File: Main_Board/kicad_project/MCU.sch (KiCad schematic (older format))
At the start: 3 parts

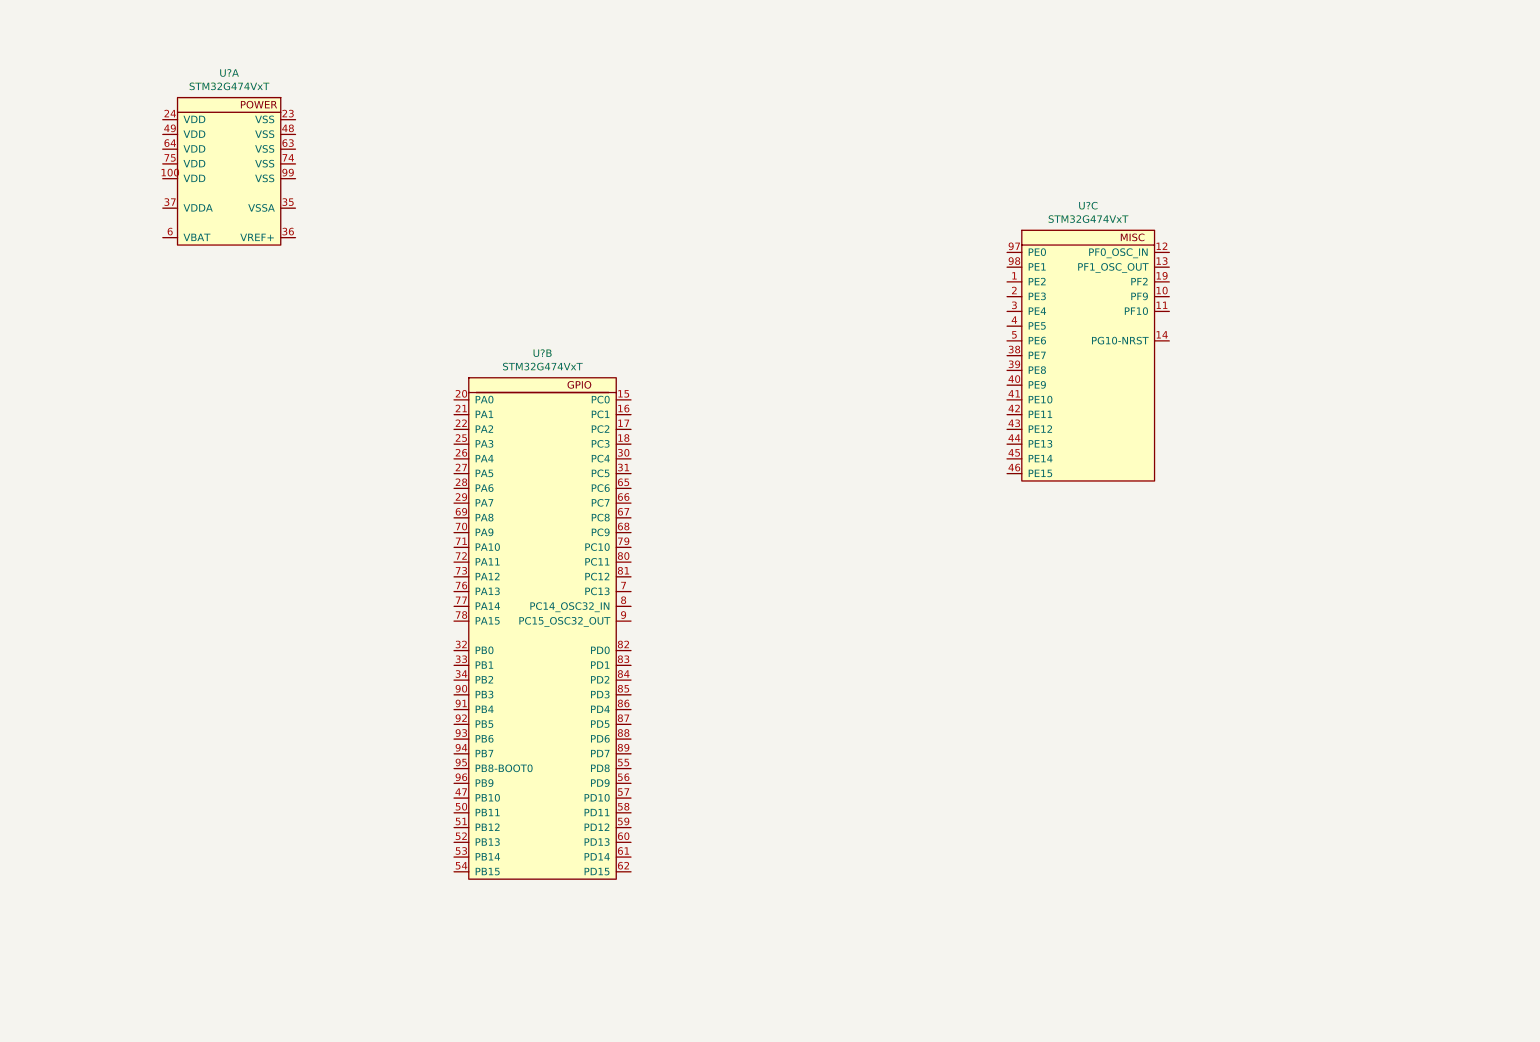
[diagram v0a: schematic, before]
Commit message: add input/output schematic, add documentation
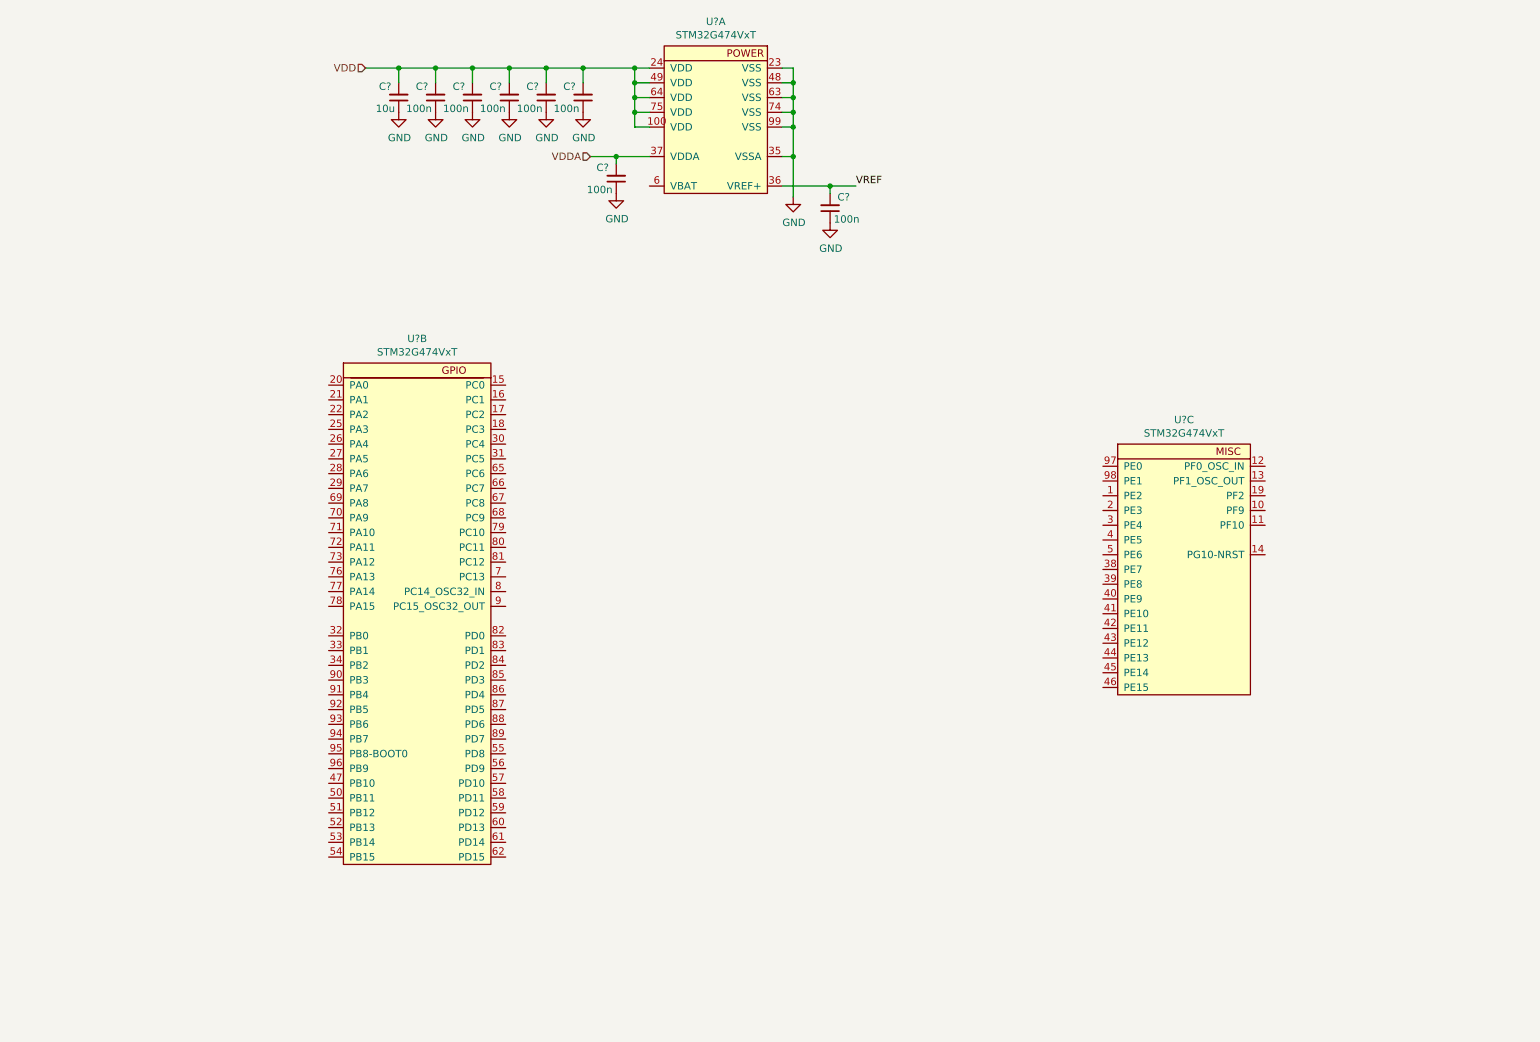
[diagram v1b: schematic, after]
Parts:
- added C? (x7): 100n, Capacitor_SMD:C_0603_1608Metric, symbol Device:C_Small
- added C?: 10u, Capacitor_SMD:C_1210_3225Metri, symbol Device:C_Small
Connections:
- net VDD: now reaches U?.100 (VDD)
- net VDD: now also U?.24 (VDD), U?.49 (VDD), U?.64 (VDD), U?.75 (VDD), C?.2, C?.2, C?.2, C?.2, C?.2, C?.2
- net GND: now reaches U?.23 (VSS)
- net GND: now also U?.35 (VSSA), U?.48 (VSS), U?.63 (VSS), U?.74 (VSS), U?.99 (VSS), C?.1, C?.1, C?.1, C?.1, C?.1, C?.1, C?.1, C?.1
- net VREF: now reaches U?.36 (VREF+)
- net VREF: now also C?.2
- net VDDA: now reaches U?.37 (VDDA)
- net VDDA: now also C?.2
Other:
- moved on the sheet: U?A, U?B, U?C

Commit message: add external IO
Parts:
- C?: footprint Capacitor_SMD:C_1210_3225Metri -> Capacitor_SMD:C_1210_3225Metric
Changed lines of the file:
@@
 $Descr A4 11693 8268
 encoding utf-8
-Sheet 7 8
+Sheet 7 9
 Title ""
 Date ""
@@
 F 0 "C?" H 3275 975 50  0000 R CNN
 F 1 "10u" H 3300 1125 50  0000 R CNN
-F 2 "Capacitor_SMD:C_1210_3225Metri" H 3325 1050 50  0001 C CNN
+F 2 "Capacitor_SMD:C_1210_3225Metric" H 3325 1050 50  0001 C CNN
 F 3 "~" H 3325 1050 50  0001 C CNN
 	1    3325 1050

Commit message: progress?
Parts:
- gave numbers to parts that had none: 9
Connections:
- net USB_DM: now reaches U7.72 (PA11)
- net USB_DP: now reaches U7.73 (PA12)
- net SWDIO_JTMS: now reaches U7.76 (PA13)
- net SWCLK_JTCK: now reaches U7.77 (PA14)
- net JDI: now reaches U7.78 (PA15)
- net JTDO_TRACESWO: now reaches U7.90 (PB3)
- net JTRST: now reaches U7.91 (PB4)
- net NRST: now reaches U7.14 (PG10-NRST)
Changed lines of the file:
@@
 $EndDescr
 $Comp
-L LoaDy:STM32G474VxT U?
+L LoaDy:STM32G474VxT U7
 U 1 1 5F5465C4
 P 5475 1250
-F 0 "U?" H 5475 1965 50  0000 C CNN
+F 0 "U7" H 5475 1965 50  0000 C CNN
 F 1 "STM32G474VxT" H 5475 1874 50  0000 C CNN
 F 2 "Package_QFP:LQFP-100_14x14mm_P0.5mm" H 5475 1950 50  0001 C CNN
@@
 $EndComp
 $Comp
-L LoaDy:STM32G474VxT U?
+L LoaDy:STM32G474VxT U7
 U 2 1 5F547F4E
 P 3450 3400
-F 0 "U?" H 3450 4115 50  0000 C CNN
+F 0 "U7" H 3450 4115 50  0000 C CNN
 F 1 "STM32G474VxT" H 3450 4024 50  0000 C CNN
 F 2 "Package_QFP:LQFP-100_14x14mm_P0.5mm" H 3450 4100 50  0001 C CNN
@@
 $EndComp
 $Comp
-L LoaDy:STM32G474VxT U?
+L LoaDy:STM32G474VxT U7
 U 3 1 5F54AE3E
 P 8650 3950
-F 0 "U?" H 8650 4665 50  0000 C CNN
+F 0 "U7" H 8650 4665 50  0000 C CNN
 F 1 "STM32G474VxT" H 8650 4574 50  0000 C CNN
 F 2 "Package_QFP:LQFP-100_14x14mm_P0.5mm" H 8650 4650 50  0001 C CNN
@@
 $EndComp
 $Comp
-L Device:C_Small C?
+L Device:C_Small C60
 U 1 1 5F50168E
 P 4575 1050
-F 0 "C?" H 4525 975 50  0000 R CNN
+F 0 "C60" H 4525 975 50  0000 R CNN
 F 1 "100n" H 4550 1125 50  0000 R CNN
 F 2 "Capacitor_SMD:C_0603_1608Metric" H 4575 1050 50  0001 C CNN
@@
 $EndComp
 $Comp
-L Device:C_Small C?
+L Device:C_Small C59
 U 1 1 5F503E90
 P 4325 1050
-F 0 "C?" H 4275 975 50  0000 R CNN
+F 0 "C59" H 4275 975 50  0000 R CNN
 F 1 "100n" H 4300 1125 50  0000 R CNN
 F 2 "Capacitor_SMD:C_0603_1608Metric" H 4325 1050 50  0001 C CNN
@@
 $EndComp
 $Comp
-L Device:C_Small C?
+L Device:C_Small C58
 U 1 1 5F504272
 P 4075 1050
-F 0 "C?" H 4025 975 50  0000 R CNN
+F 0 "C58" H 4025 975 50  0000 R CNN
 F 1 "100n" H 4050 1125 50  0000 R CNN
 F 2 "Capacitor_SMD:C_0603_1608Metric" H 4075 1050 50  0001 C CNN
@@
 $EndComp
 $Comp
-L Device:C_Small C?
+L Device:C_Small C57
 U 1 1 5F50454D
 P 3825 1050
-F 0 "C?" H 3775 975 50  0000 R CNN
+F 0 "C57" H 3775 975 50  0000 R CNN
 F 1 "100n" H 3800 1125 50  0000 R CNN
 F 2 "Capacitor_SMD:C_0603_1608Metric" H 3825 1050 50  0001 C CNN
@@
 $EndComp
 $Comp
-L Device:C_Small C?
+L Device:C_Small C56
 U 1 1 5F504BCE
 P 3575 1050
-F 0 "C?" H 3525 975 50  0000 R CNN
+F 0 "C56" H 3525 975 50  0000 R CNN
 F 1 "100n" H 3550 1125 50  0000 R CNN
 F 2 "Capacitor_SMD:C_0603_1608Metric" H 3575 1050 50  0001 C CNN
@@
 $EndComp
 $Comp
-L Device:C_Small C?
+L Device:C_Small C55
 U 1 1 5F505049
 P 3325 1050
-F 0 "C?" H 3275 975 50  0000 R CNN
+F 0 "C55" H 3275 975 50  0000 R CNN
 F 1 "10u" H 3300 1125 50  0000 R CNN
 F 2 "Capacitor_SMD:C_1210_3225Metric" H 3325 1050 50  0001 C CNN
@@
 	4925 1150 4925 1050
 $Comp
-L power:GND #PWR?
+L power:GND #PWR050
 U 1 1 5F508D68
 P 4575 1150
-F 0 "#PWR?" H 4575 900 50  0001 C CNN
+F 0 "#PWR050" H 4575 900 50  0001 C CNN
 F 1 "GND" H 4580 977 50  0000 C CNN
 F 2 "" H 4575 1150 50  0001 C CNN
@@
 $EndComp
 $Comp
-L power:GND #PWR?
+L power:GND #PWR049
 U 1 1 5F5090A8
 P 4325 1150
-F 0 "#PWR?" H 4325 900 50  0001 C CNN
+F 0 "#PWR049" H 4325 900 50  0001 C CNN
 F 1 "GND" H 4330 977 50  0000 C CNN
 F 2 "" H 4325 1150 50  0001 C CNN
@@
 $EndComp
 $Comp
-L power:GND #PWR?
+L power:GND #PWR048
 U 1 1 5F5092B8
 P 4075 1150
-F 0 "#PWR?" H 4075 900 50  0001 C CNN
+F 0 "#PWR048" H 4075 900 50  0001 C CNN
 F 1 "GND" H 4080 977 50  0000 C CNN
 F 2 "" H 4075 1150 50  0001 C CNN
@@
 $EndComp
 $Comp
-L power:GND #PWR?
+L power:GND #PWR047
 U 1 1 5F509567
 P 3825 1150
-F 0 "#PWR?" H 3825 900 50  0001 C CNN
+F 0 "#PWR047" H 3825 900 50  0001 C CNN
 F 1 "GND" H 3830 977 50  0000 C CNN
 F 2 "" H 3825 1150 50  0001 C CNN
@@
 $EndComp
 $Comp
-L power:GND #PWR?
+L power:GND #PWR046
 U 1 1 5F5097C9
 P 3575 1150
-F 0 "#PWR?" H 3575 900 50  0001 C CNN
+F 0 "#PWR046" H 3575 900 50  0001 C CNN
 F 1 "GND" H 3580 977 50  0000 C CNN
 F 2 "" H 3575 1150 50  0001 C CNN
@@
 $EndComp
 $Comp
-L power:GND #PWR?
+L power:GND #PWR045
 U 1 1 5F50999B
 P 3325 1150
-F 0 "#PWR?" H 3325 900 50  0001 C CNN
+F 0 "#PWR045" H 3325 900 50  0001 C CNN
 F 1 "GND" H 3330 977 50  0000 C CNN
 F 2 "" H 3325 1150 50  0001 C CNN
@@
 VDD
 $Comp
-L Device:C_Small C?
+L Device:C_Small C61
 U 1 1 5F509E58
 P 4800 1600
-F 0 "C?" H 4750 1525 50  0000 R CNN
+F 0 "C61" H 4750 1525 50  0000 R CNN
 F 1 "100n" H 4775 1675 50  0000 R CNN
 F 2 "Capacitor_SMD:C_0603_1608Metric" H 4800 1600 50  0001 C CNN
@@
 $EndComp
 $Comp
-L power:GND #PWR?
+L power:GND #PWR051
 U 1 1 5F50A4F3
 P 4800 1700
-F 0 "#PWR?" H 4800 1450 50  0001 C CNN
+F 0 "#PWR051" H 4800 1450 50  0001 C CNN
 F 1 "GND" H 4805 1527 50  0000 C CNN
 F 2 "" H 4800 1700 50  0001 C CNN
@@
 VDDA
 $Comp
-L power:GND #PWR?
+L power:GND #PWR052
 U 1 1 5F513C8D
 P 6000 1725
-F 0 "#PWR?" H 6000 1475 50  0001 C CNN
+F 0 "#PWR052" H 6000 1475 50  0001 C CNN
 F 1 "GND" H 6005 1552 50  0000 C CNN
 F 2 "" H 6000 1725 50  0001 C CNN
@@
 	6000 1450 6000 1250
 $Comp
-L Device:C_Small C?
+L Device:C_Small C62
 U 1 1 5F517AF6
 P 6250 1800
-F 0 "C?" H 6200 1725 50  0000 R CNN
+F 0 "C62" H 6200 1725 50  0000 R CNN
 F 1 "100n" H 6225 1875 50  0000 R CNN
 F 2 "Capacitor_SMD:C_0603_1608Metric" H 6250 1800 50  0001 C CNN
@@
 	5925 1650 6250 1650
 $Comp
-L power:GND #PWR?
+L power:GND #PWR053
 U 1 1 5F51901D
 P 6250 1900
-F 0 "#PWR?" H 6250 1650 50  0001 C CNN
+F 0 "#PWR053" H 6250 1650 50  0001 C CNN
 F 1 "GND" H 6255 1727 50  0000 C CNN
 F 2 "" H 6250 1900 50  0001 C CNN
@@
 Text Label 6425 1650 0    50   ~ 0
 VREF
+Wire Wire Line
+	2850 4100 2500 4100
+Wire Wire Line
+	2850 4200 2500 4200
+Text Label 2725 4100 2    50   ~ 0
+USB_DM
+Text Label 2700 4200 2    50   ~ 0
+USB_DP
+Wire Wire Line
+	2850 4300 2500 4300
+Wire Wire Line
+	2850 4400 2500 4400
+Text Label 2500 4300 2    50   ~ 0
+SWDIO_JTMS
+Text Label 2500 4400 2    50   ~ 0
+SWCLK_JTCK
+Wire Wire Line
+	2500 4500 2850 4500
+Text Label 2500 4500 2    50   ~ 0
+JDI
+Wire Wire Line
+	2850 5000 2500 5000
+Text Label 2500 5000 2    50   ~ 0
+JTDO_TRACESWO
+Wire Wire Line
+	2850 5100 2500 5100
+Text Label 2500 5100 2    50   ~ 0
+JTRST
+Wire Wire Line
+	9200 4150 9450 4150
+Text Label 9450 4150 0    50   ~ 0
+NRST
+Entry Wire Line
+	2500 4100 2400 4000
+Entry Wire Line
+	2500 4200 2400 4100
+Wire Bus Line
+	2400 3875 2300 3875
+Wire Bus Line
+	2400 3875 2400 4100
+Text HLabel 2300 3875 0    50   BiDi ~ 10
+USB
 $EndSCHEMATC

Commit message: progress on MCU pinout
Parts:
- renumbered C60 to C?, C59 to C?, C58 to C?, C57 to C?, C56 to C?, C55 to C?, C61 to C?, C62 to C?, U7 to U?
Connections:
- net MCO: now reaches U?.69 (PA8)
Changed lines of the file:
@@
 $EndDescr
 $Comp
-L LoaDy:STM32G474VxT U7
+L LoaDy:STM32G474VxT U?
 U 1 1 5F5465C4
 P 5475 1250
-F 0 "U7" H 5475 1965 50  0000 C CNN
+F 0 "U?" H 5475 1965 50  0000 C CNN
 F 1 "STM32G474VxT" H 5475 1874 50  0000 C CNN
 F 2 "Package_QFP:LQFP-100_14x14mm_P0.5mm" H 5475 1950 50  0001 C CNN
@@
 $EndComp
 $Comp
-L LoaDy:STM32G474VxT U7
+L LoaDy:STM32G474VxT U?
 U 2 1 5F547F4E
 P 3450 3400
-F 0 "U7" H 3450 4115 50  0000 C CNN
+F 0 "U?" H 3450 4115 50  0000 C CNN
 F 1 "STM32G474VxT" H 3450 4024 50  0000 C CNN
 F 2 "Package_QFP:LQFP-100_14x14mm_P0.5mm" H 3450 4100 50  0001 C CNN
@@
 $EndComp
 $Comp
-L LoaDy:STM32G474VxT U7
+L LoaDy:STM32G474VxT U?
 U 3 1 5F54AE3E
 P 8650 3950
-F 0 "U7" H 8650 4665 50  0000 C CNN
+F 0 "U?" H 8650 4665 50  0000 C CNN
 F 1 "STM32G474VxT" H 8650 4574 50  0000 C CNN
 F 2 "Package_QFP:LQFP-100_14x14mm_P0.5mm" H 8650 4650 50  0001 C CNN
@@
 $EndComp
 $Comp
-L Device:C_Small C60
+L Device:C_Small C?
 U 1 1 5F50168E
 P 4575 1050
-F 0 "C60" H 4525 975 50  0000 R CNN
+F 0 "C?" H 4525 975 50  0000 R CNN
 F 1 "100n" H 4550 1125 50  0000 R CNN
 F 2 "Capacitor_SMD:C_0603_1608Metric" H 4575 1050 50  0001 C CNN
@@
 $EndComp
 $Comp
-L Device:C_Small C59
+L Device:C_Small C?
 U 1 1 5F503E90
 P 4325 1050
-F 0 "C59" H 4275 975 50  0000 R CNN
+F 0 "C?" H 4275 975 50  0000 R CNN
 F 1 "100n" H 4300 1125 50  0000 R CNN
 F 2 "Capacitor_SMD:C_0603_1608Metric" H 4325 1050 50  0001 C CNN
@@
 $EndComp
 $Comp
-L Device:C_Small C58
+L Device:C_Small C?
 U 1 1 5F504272
 P 4075 1050
-F 0 "C58" H 4025 975 50  0000 R CNN
+F 0 "C?" H 4025 975 50  0000 R CNN
 F 1 "100n" H 4050 1125 50  0000 R CNN
 F 2 "Capacitor_SMD:C_0603_1608Metric" H 4075 1050 50  0001 C CNN
@@
 $EndComp
 $Comp
-L Device:C_Small C57
+L Device:C_Small C?
 U 1 1 5F50454D
 P 3825 1050
-F 0 "C57" H 3775 975 50  0000 R CNN
+F 0 "C?" H 3775 975 50  0000 R CNN
 F 1 "100n" H 3800 1125 50  0000 R CNN
 F 2 "Capacitor_SMD:C_0603_1608Metric" H 3825 1050 50  0001 C CNN
@@
 $EndComp
 $Comp
-L Device:C_Small C56
+L Device:C_Small C?
 U 1 1 5F504BCE
 P 3575 1050
-F 0 "C56" H 3525 975 50  0000 R CNN
+F 0 "C?" H 3525 975 50  0000 R CNN
 F 1 "100n" H 3550 1125 50  0000 R CNN
 F 2 "Capacitor_SMD:C_0603_1608Metric" H 3575 1050 50  0001 C CNN
@@
 $EndComp
 $Comp
-L Device:C_Small C55
+L Device:C_Small C?
 U 1 1 5F505049
 P 3325 1050
-F 0 "C55" H 3275 975 50  0000 R CNN
+F 0 "C?" H 3275 975 50  0000 R CNN
 F 1 "10u" H 3300 1125 50  0000 R CNN
 F 2 "Capacitor_SMD:C_1210_3225Metric" H 3325 1050 50  0001 C CNN
@@
 	4925 1150 4925 1050
 $Comp
-L power:GND #PWR050
+L power:GND #PWR?
 U 1 1 5F508D68
 P 4575 1150
-F 0 "#PWR050" H 4575 900 50  0001 C CNN
+F 0 "#PWR?" H 4575 900 50  0001 C CNN
 F 1 "GND" H 4580 977 50  0000 C CNN
 F 2 "" H 4575 1150 50  0001 C CNN
@@
 $EndComp
 $Comp
-L power:GND #PWR049
+L power:GND #PWR?
 U 1 1 5F5090A8
 P 4325 1150
-F 0 "#PWR049" H 4325 900 50  0001 C CNN
+F 0 "#PWR?" H 4325 900 50  0001 C CNN
 F 1 "GND" H 4330 977 50  0000 C CNN
 F 2 "" H 4325 1150 50  0001 C CNN
@@
 $EndComp
 $Comp
-L power:GND #PWR048
+L power:GND #PWR?
 U 1 1 5F5092B8
 P 4075 1150
-F 0 "#PWR048" H 4075 900 50  0001 C CNN
+F 0 "#PWR?" H 4075 900 50  0001 C CNN
 F 1 "GND" H 4080 977 50  0000 C CNN
 F 2 "" H 4075 1150 50  0001 C CNN
@@
 $EndComp
 $Comp
-L power:GND #PWR047
+L power:GND #PWR?
 U 1 1 5F509567
 P 3825 1150
-F 0 "#PWR047" H 3825 900 50  0001 C CNN
+F 0 "#PWR?" H 3825 900 50  0001 C CNN
 F 1 "GND" H 3830 977 50  0000 C CNN
 F 2 "" H 3825 1150 50  0001 C CNN
@@
 $EndComp
 $Comp
-L power:GND #PWR046
+L power:GND #PWR?
 U 1 1 5F5097C9
 P 3575 1150
-F 0 "#PWR046" H 3575 900 50  0001 C CNN
+F 0 "#PWR?" H 3575 900 50  0001 C CNN
 F 1 "GND" H 3580 977 50  0000 C CNN
 F 2 "" H 3575 1150 50  0001 C CNN
@@
 $EndComp
 $Comp
-L power:GND #PWR045
+L power:GND #PWR?
 U 1 1 5F50999B
 P 3325 1150
-F 0 "#PWR045" H 3325 900 50  0001 C CNN
+F 0 "#PWR?" H 3325 900 50  0001 C CNN
 F 1 "GND" H 3330 977 50  0000 C CNN
 F 2 "" H 3325 1150 50  0001 C CNN
@@
 VDD
 $Comp
-L Device:C_Small C61
+L Device:C_Small C?
 U 1 1 5F509E58
 P 4800 1600
-F 0 "C61" H 4750 1525 50  0000 R CNN
+F 0 "C?" H 4750 1525 50  0000 R CNN
 F 1 "100n" H 4775 1675 50  0000 R CNN
 F 2 "Capacitor_SMD:C_0603_1608Metric" H 4800 1600 50  0001 C CNN
@@
 $EndComp
 $Comp
-L power:GND #PWR051
+L power:GND #PWR?
 U 1 1 5F50A4F3
 P 4800 1700
-F 0 "#PWR051" H 4800 1450 50  0001 C CNN
+F 0 "#PWR?" H 4800 1450 50  0001 C CNN
 F 1 "GND" H 4805 1527 50  0000 C CNN
 F 2 "" H 4800 1700 50  0001 C CNN
@@
 VDDA
 $Comp
-L power:GND #PWR052
+L power:GND #PWR?
 U 1 1 5F513C8D
 P 6000 1725
-F 0 "#PWR052" H 6000 1475 50  0001 C CNN
+F 0 "#PWR?" H 6000 1475 50  0001 C CNN
 F 1 "GND" H 6005 1552 50  0000 C CNN
 F 2 "" H 6000 1725 50  0001 C CNN
@@
 	6000 1450 6000 1250
 $Comp
-L Device:C_Small C62
+L Device:C_Small C?
 U 1 1 5F517AF6
 P 6250 1800
-F 0 "C62" H 6200 1725 50  0000 R CNN
+F 0 "C?" H 6200 1725 50  0000 R CNN
 F 1 "100n" H 6225 1875 50  0000 R CNN
 F 2 "Capacitor_SMD:C_0603_1608Metric" H 6250 1800 50  0001 C CNN
@@
 	5925 1650 6250 1650
 $Comp
-L power:GND #PWR053
+L power:GND #PWR?
 U 1 1 5F51901D
 P 6250 1900
-F 0 "#PWR053" H 6250 1650 50  0001 C CNN
+F 0 "#PWR?" H 6250 1650 50  0001 C CNN
 F 1 "GND" H 6255 1727 50  0000 C CNN
 F 2 "" H 6250 1900 50  0001 C CNN
@@
 Wire Wire Line
 	2850 4200 2500 4200
-Text Label 2725 4100 2    50   ~ 0
+Text Label 2500 4100 2    50   ~ 0
 USB_DM
-Text Label 2700 4200 2    50   ~ 0
+Text Label 2500 4200 2    50   ~ 0
 USB_DP
 Wire Wire Line
@@
 Text Label 9450 4150 0    50   ~ 0
 NRST
-Entry Wire Line
-	2500 4100 2400 4000
-Entry Wire Line
-	2500 4200 2400 4100
-Wire Bus Line
-	2400 3875 2300 3875
-Wire Bus Line
-	2400 3875 2400 4100
-Text HLabel 2300 3875 0    50   BiDi ~ 10
-USB
+Text Label 2500 3800 2    50   ~ 0
+MCO
+Wire Wire Line
+	2500 3800 2850 3800
 $EndSCHEMATC
